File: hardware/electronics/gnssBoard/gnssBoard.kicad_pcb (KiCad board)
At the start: 4 copper layers, 0 parts

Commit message: worked on GNSS board
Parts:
- added AE1: CONMHF1-SMD-T, lib_fp:CONMHF1, F.Cu at (148.5, 80.5)
- added BT1: ~, lib_fp:MS621FE-FL11E, F.Cu at (132.9, 81.7)
- added C1: 2.2uF, lib_fp:MLCC0603, F.Cu at (147.7, 112.8)
- added C10: 10nF, lib_fp:MLCC0603, F.Cu at (146.3, 84.2)
- added C2: 2.2uF, lib_fp:MLCC0603, F.Cu at (142.2, 112.5)
- added C3: 1uF, lib_fp:MLCC0603, F.Cu at (130.2, 92.1)
- added C4: 100nF, lib_fp:MLCC0603, F.Cu at (130.2, 95.0)
- added C5: 100nF, lib_fp:MLCC0603, F.Cu at (130.2, 98.0)
- added C6: 1uF, lib_fp:MLCC0603, F.Cu at (130.2, 101.0)
- added C7: 100nF, lib_fp:MLCC0603, F.Cu at (130.2, 103.9)
- added C8: 2.2uF, lib_fp:MLCC0603, F.Cu at (135.8, 85.8)
- added C9: 47pF, lib_fp:MLCC0603, F.Cu at (149.8, 104.8)
- added D1: LTST-C190KYKT, lib_fp:LTST-0603, F.Cu at (130.0, 113.6)
- added D2: LTST-C190KGKT, lib_fp:LTST-0603, F.Cu at (140.2, 79.1)
- added D3: LTST-C190KRKT, lib_fp:LTST-0603, F.Cu at (140.2, 80.7)
- added D4: LTST-C190TBKT, lib_fp:LTST-0603, F.Cu at (149.8, 108.4)
- added D5: B0540WQ, lib_fp:SOD123, F.Cu at (138.6, 84.9)
- added D6: PTVS4V5D1BLYL, lib_fp:SOD882, F.Cu at (148.2, 83.6)
- added J2: M.2_E_Key_PCB_Edge, lib_fp:M.2 E-Key, F.Cu at (140.0, 120.0)
- added JP1: ~, lib_fp:Jumper_2_Bridged, B.Cu at (176.6, 100.8)
- added JP4: ~, lib_fp:Jumper_2_Bridged, B.Cu at (176.4, 104.5)
- added L1: 47nH, lib_fp:L_0402, F.Cu at (148.1, 85.0)
- added Q1: DMN2992UFB4Q-7B, lib_fp:XDFN3P35_100X60X40L15X25N, F.Cu at (135.6, 114.4)
- added Q2: DMN2992UFB4Q-7B, lib_fp:XDFN3P35_100X60X40L15X25N, F.Cu at (136.7, 114.4)
- added Q3: DMN2992UFB4Q-7B, lib_fp:XDFN3P35_100X60X40L15X25N, F.Cu at (134.5, 114.4)
- added Q4: DMN2992UFB4Q-7B, lib_fp:XDFN3P35_100X60X40L15X25N, F.Cu at (133.4, 114.4)
- added Q5: DMG1013TQ-7, lib_fp:SOT23-3P50_160X160X75L22X22N, F.Cu at (146.5, 86.8)
- added R1: 10K, lib_fp:CRCW0402, F.Cu at (144.8, 115.0)
- added R10: 4K7, lib_fp:CRCW0402, F.Cu at (134.5, 112.2)
- added R11: 4K7, lib_fp:CRCW0402, F.Cu at (133.4, 112.2)
- added R12: 4K7, lib_fp:CRCW0402, F.Cu at (120.9, 117.4)
- added R13: 4K7, lib_fp:CRCW0402, F.Cu at (120.9, 119.5)
- added R14: 4K7, lib_fp:CRCW0402, F.Cu at (149.8, 111.0)
- added R15: 3K3, lib_fp:CRCW0402, F.Cu at (135.3, 87.2)
- added R16: 10R, lib_fp:CRCW0603, F.Cu at (144.7, 85.8)
- added R17: 10K, lib_fp:CRCW0402, F.Cu at (148.2, 86.8)
- added R18: 1K, lib_fp:CRCW0402, F.Cu at (142.0, 86.5)
- added R19: 100K, lib_fp:CRCW0402, F.Cu at (140.2, 86.5)
- added R2: 10K, lib_fp:CRCW0402, F.Cu at (146.8, 115.0)
- added R20: 10K, lib_fp:CRCW0402, F.Cu at (140.8, 111.9)
- added R21: 27R, lib_fp:CRCW0402, F.Cu at (150.2, 113.5)
- added R22: 27R, lib_fp:CRCW0402, F.Cu at (149.0, 113.5)
- added R23: 10K, lib_fp:CRCW0402, F.Cu at (139.6, 111.9)
- added R3: 1K, lib_fp:CRCW0402, F.Cu at (130.5, 111.5)
- added R4: 4K7, lib_fp:CRCW0402, F.Cu at (137.6, 79.1)
- added R5: 4K7, lib_fp:CRCW0402, F.Cu at (137.6, 80.7)
- added R6: 4K7, lib_fp:CRCW0402, F.Cu at (136.7, 112.2)
- added R7: 4K7, lib_fp:CRCW0402, F.Cu at (135.6, 112.2)
- added R8: 4K7, lib_fp:CRCW0402, F.Cu at (119.2, 110.4)
- added R9: 4K7, lib_fp:CRCW0402, F.Cu at (119.2, 112.5)
- added TP1: ~, lib_fp:TP_1mm, B.Cu at (179.4, 83.8)
- added TP10: ~, lib_fp:TP_1mm, B.Cu at (177.4, 91.8)
- added TP11: ~, lib_fp:TP_1mm, B.Cu at (178.7, 95.2)
- added TP12: ~, lib_fp:TP_1mm, B.Cu at (178.7, 97.2)
- added TP13: ~, lib_fp:TP_1mm, B.Cu at (176.7, 95.2)
- added TP14: ~, lib_fp:TP_1mm, B.Cu at (176.7, 97.2)
- added TP15: ~, lib_fp:TP_1mm, B.Cu at (174.7, 95.2)
- added TP16: ~, lib_fp:TP_1mm, B.Cu at (174.7, 97.2)
- added TP2: ~, lib_fp:TP_1mm, B.Cu at (179.4, 85.8)
- added TP3: ~, lib_fp:TP_1mm, B.Cu at (179.4, 87.8)
- added TP4: ~, lib_fp:TP_1mm, B.Cu at (179.4, 89.8)
- added TP5: ~, lib_fp:TP_1mm, B.Cu at (179.4, 91.8)
- added TP6: ~, lib_fp:TP_1mm, B.Cu at (177.4, 83.8)
- added TP7: ~, lib_fp:TP_1mm, B.Cu at (177.4, 85.8)
- added TP8: ~, lib_fp:TP_1mm, B.Cu at (177.4, 87.8)
- added TP9: ~, lib_fp:TP_1mm, B.Cu at (177.4, 89.8)
- added U1: AP7361E, lib_fp:UDFN8P65_300X300X60L25X45L, F.Cu at (144.9, 112.8)
- added U2: ZED-F9P, lib_fp:ZED-F9P-04B_UBL, F.Cu at (140.0, 99.5)
- added U3: OPA344, lib_fp:SOT23-5P95_280X300X110L40X38N, F.Cu at (142.0, 84.0)
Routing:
- net +3V3: track 0.00 -> 79.1 mm, vias 0 -> 9
- net Net-(J2-~{LED_1}): track 0.00 -> 43.7 mm, vias 0 -> 3
- net Net-(J2-~{LED_2}): track 0.00 -> 43.4 mm, vias 0 -> 3
- net /GNSS Module/ANT_DET: track 0.00 -> 29.9 mm, vias 0 -> 2
- net /GNSS Module/ZED_D-: track 0.00 -> 27.6 mm, vias 0 -> 2
- net /GNSS Module/ZED_D+: track 0.00 -> 27.0 mm, vias 0 -> 2
- net VSS: track 0.00 -> 24.0 mm, vias 0 -> 94
- net /GNSS Module/ANT_SHORT_N: track 0.00 -> 21.9 mm, vias 0 -> 2
- net /GNSS Module/ANT_IN: track 0.00 -> 21.1 mm
- net VBAT: track 0.00 -> 19.4 mm, vias 0 -> 2
- net /PPS: track 0.00 -> 18.3 mm, vias 0 -> 1
- net /GNSS Module/ANT_OFF: track 0.00 -> 17.7 mm, vias 0 -> 2
- net VCC_RF: track 0.00 -> 16.4 mm, vias 0 -> 2
- net /ZED_RXD_1V8: track 0.00 -> 14.0 mm, vias 0 -> 3
- net /ZED_TXD_1V8: track 0.00 -> 13.2 mm, vias 0 -> 3
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- added copper zone on B.Cu, net +3V3
- added copper zone on F.Cu, net VSS
- added copper zone on In1.Cu, net VSS
- added copper zone on In2.Cu, net VSS
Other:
- board outline added: 22 x 36.8 mm

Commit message: finished first attempt at layout
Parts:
- removed JP1, JP4: ~, lib_fp:Jumper_2_Bridged
- removed TP1, TP10, TP11, TP12, TP13, TP14, TP15, TP16, TP2, TP3, TP4, TP5, TP6, TP7, TP8, TP9: ~, lib_fp:TP_1mm
- moved R9 15.8 mm to (134.7, 115.4)
- moved R8 13.1 mm to (131.6, 114.9), turned to -90 degrees
- moved R13 13.1 mm to (130.2, 110.2)
- moved R12 12.1 mm to (132.7, 114.9), turned to -90 degrees
- moved Q1 3.51 mm to (138.6, 112.5)
- moved Q4 2.62 mm to (132.1, 112.1)
- moved Q3 0.65 mm to (133.9, 114.0)
- moved Q2 0.65 mm to (136.2, 114.0)
- moved R3 0.33 mm to (130.2, 111.4)
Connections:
- D1 pad 2: Net-(D1-Pad2) -> VSS
- D4 pad 2: Net-(D4-Pad2) -> VSS
- J2 pad 40: /RESET_N -> /EXTINT
- J2 pad 42: /EXTINT -> /RESET_N
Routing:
- net +3V3: track 79.1 -> 129.6 mm, vias 9 -> 11
- net +1V8: track 12.1 -> 38.4 mm, vias 4 -> 5
- net /SCL_1V8: track 4.58 -> 17.3 mm, vias 1 -> 2
- net VSS: track 24.0 -> 36.7 mm, vias 94 -> 93
- net /ZED_TXD_1V8: track 13.2 -> 20.2 mm, vias 3 -> 4
- net /GNSS Module/SDA_3V3: track 2.29 -> 6.08 mm, vias 1 -> 2
- net /GNSS Module/SCL_3V3: track 2.29 -> 5.34 mm, vias 1 -> 2
- net /ZED_RXD_1V8: track 14.0 -> 16.3 mm, vias 3 -> 4
- net /GNSS Module/ZED_TXD_3V3: track 5.41 -> 3.59 mm, vias 2 -> 0
- net /SDA_1V8: track 5.12 -> 6.15 mm
- net /EXTINT: track 12.4 -> 11.5 mm
- removed copper zone on B.Cu, net +3V3

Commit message: finished routing and passed DRC
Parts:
- added J1: VAL, lib_fp:M.2-Screw-Pad, F.Cu at (140.0, 78.0)
- moved D2 5.53 mm to (145.3, 81.2), turned to 90 degrees
- moved R5 4.92 mm to (142.2, 82.5), turned to -90 degrees
- moved R4 4.77 mm to (141.0, 82.5), turned to -90 degrees
- moved D3 3.44 mm to (143.6, 81.2), turned to 90 degrees
- moved R18 1.42 mm to (142.9, 87.6)
- moved U3 1.25 mm to (141.9, 85.3)
- moved R19 1.14 mm to (140.7, 87.6), turned to 180 degrees
- moved D5 0.46 mm to (138.6, 85.4)
- moved C9 0.30 mm to (149.8, 104.5)
- moved D4 0.05 mm to (149.8, 108.3)
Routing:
- net Net-(D2-Pad1): track 1.36 -> 7.63 mm, vias 0 -> 2
- net Net-(J2-~{LED_1}): track 43.7 -> 38.3 mm
- net +3V3: track 129.6 -> 124.6 mm, vias 11 -> 10
- net Net-(J2-~{LED_2}): track 43.4 -> 39.9 mm
- net /GNSS Module/ANT_DET: track 29.9 -> 30.8 mm
- net /GNSS Module/ANT_SHORT_N: track 21.9 -> 22.6 mm
- net Net-(D3-Pad1): track 1.36 -> 2.09 mm
- net /GNSS Module/SDA_3V3: track 6.08 -> 6.72 mm
- net VSS: vias 93 -> 96

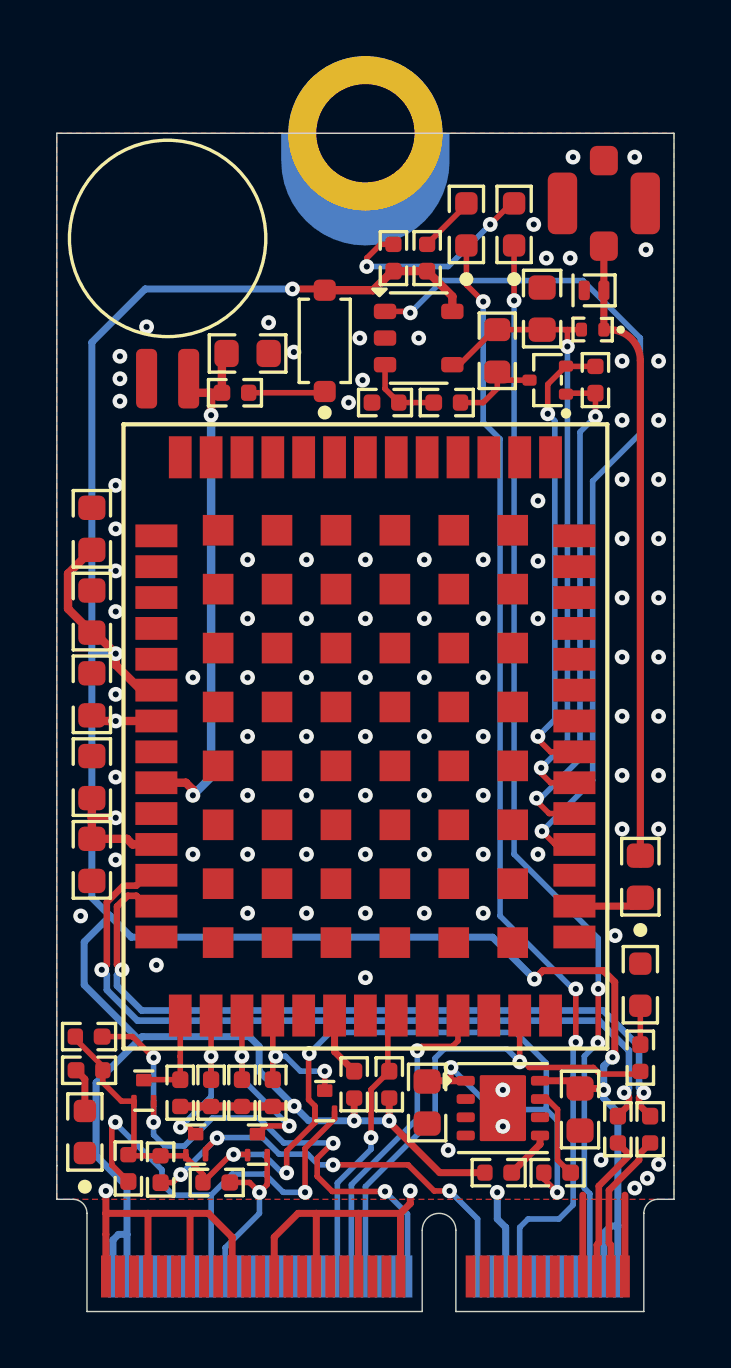
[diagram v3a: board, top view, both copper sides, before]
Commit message: replaced MOSFETS with level shifter and cleaned up routing. added silkscreen text
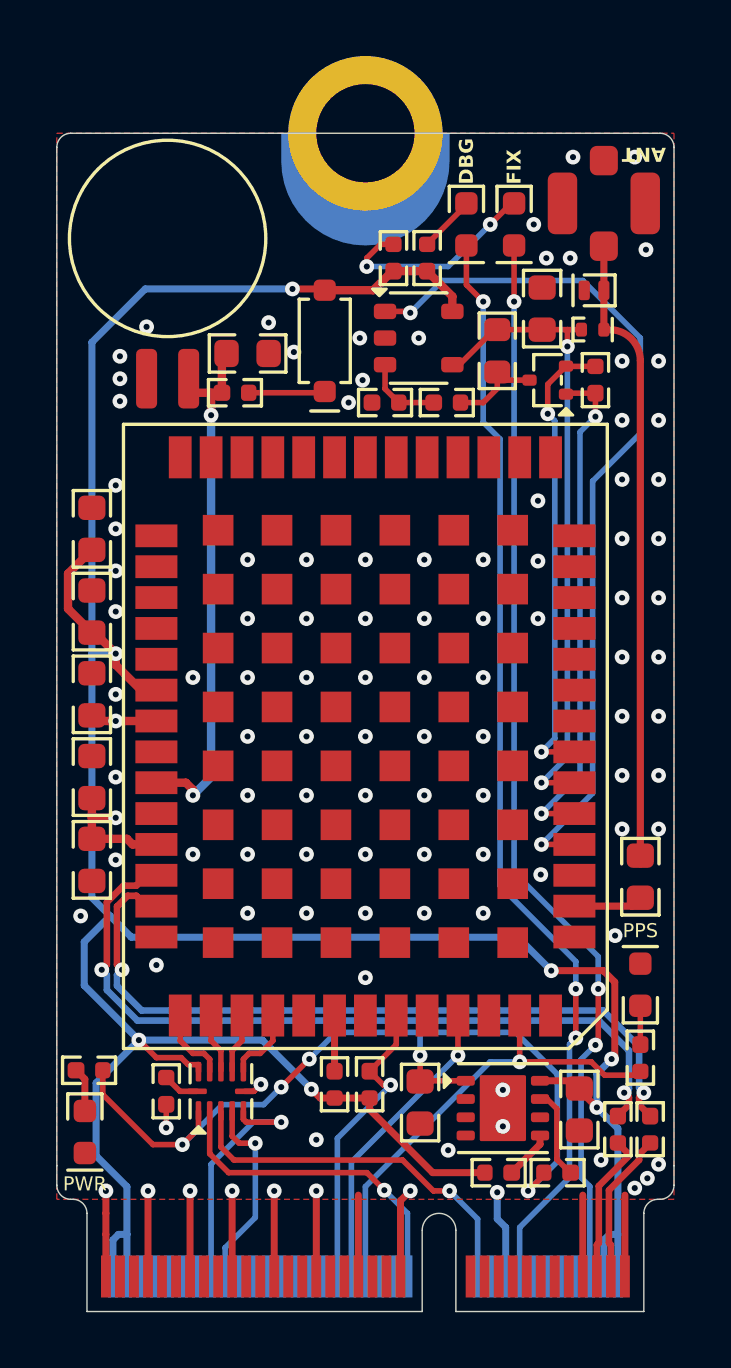
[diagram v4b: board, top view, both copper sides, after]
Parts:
- removed Q1, Q2, Q3, Q4: DMN2992UFB4Q-7B, lib_fp:XDFN3P35_100X60X40L15X25N
- removed R10, R11, R12, R13, R7, R8, R9: 4K7, lib_fp:CRCW0402
- added REF**: OSHW-Logo2_7.3x6mm_SilkScreen, DS-Logos-and-Graphics:OSHW-Logo2_7.3x6mm_SilkScreen, B.Cu at (140.0, 109.0)
- added U4: TXS0104VxRUTR, lib_fp:RUT0012A, F.Cu at (134.8, 112.2)
- R6: value 4K7 -> 10K
- moved R6 3.80 mm to (132.9, 112.2), turned to -90 degrees
- moved R20 0.70 mm to (140.2, 111.9)
- moved R23 0.70 mm to (138.9, 111.9)
- moved C2 0.25 mm to (141.9, 112.5)
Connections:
- R6 pad 1: +3V3 -> Net-(U4-OE)
- R6 pad 2: /GNSS Module/SCL_3V3 -> VSS
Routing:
- net /ZED_TXD_1V8: track 20.4 -> 11.7 mm, vias 4 -> 1
- net /SCL_1V8: track 17.4 -> 8.81 mm, vias 2 -> 1
- net +1V8: track 38.4 -> 30.4 mm
- net /GNSS Module/SDA_3V3: track 6.72 -> 2.09 mm, vias 2 -> 0
- net /GNSS Module/ZED_RXD_3V3: track 5.91 -> 2.09 mm, vias 2 -> 0
- net +3V3: track 124.6 -> 121.0 mm, vias 10 -> 9
- net /ZED_RXD_1V8: track 16.0 -> 13.5 mm, vias 4 -> 1
- net /GNSS Module/SCL_3V3: track 5.03 -> 2.67 mm, vias 2 -> 0
- net VSS: track 36.7 -> 34.8 mm, vias 96 -> 104
- net /PPS: track 18.3 -> 16.7 mm
- net Net-(U4-OE): track 0.00 -> 1.30 mm
- net /RESET_N: track 10.2 -> 11.4 mm
- net /SDA_1V8: track 6.15 -> 7.02 mm
- net Net-(J2-~{LED_2}): track 39.9 -> 39.2 mm
- net /EXTINT: track 11.5 -> 10.9 mm
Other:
- outline, holes or cut-outs redrawn
- board text added: "ANT"
- board text added: "DBG"
- board text added: "FIX"
- board text added: "PPS"
- board text added: "PWR"
- board text added: "ZED-F9P GNSS M.2 E-Key Card Embry-Riddle Aeronautical University Physical Sciences Department Madison Gleydura Master's Thesis 2024-12-01"

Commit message: re-added cut traces and test points and flxed keepout for edge connector
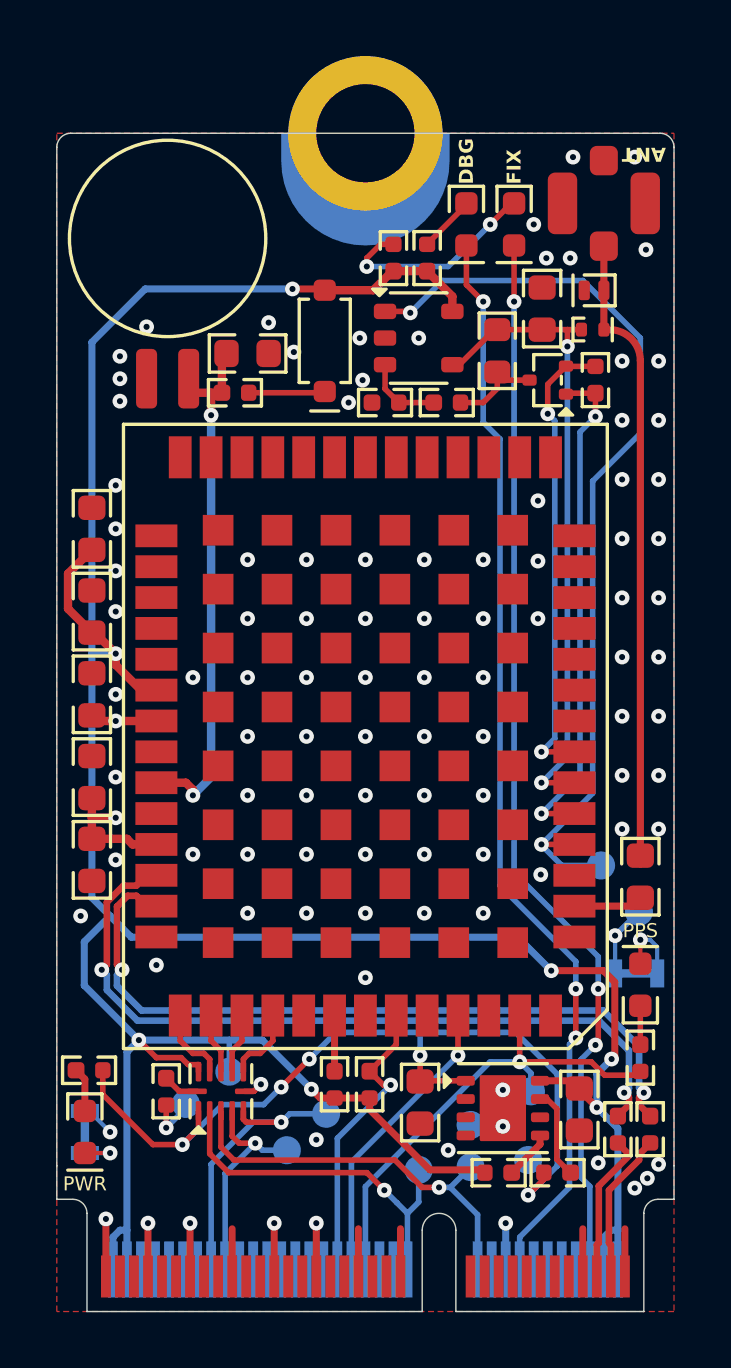
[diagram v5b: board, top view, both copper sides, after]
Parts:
- added JP1: ~, lib_fp:Jumper_2_Bridged, B.Cu at (130.0, 113.6)
- added JP2: ~, lib_fp:Jumper_2_Bridged, B.Cu at (149.7, 108.0)
- added TP1: ~, lib_fp:TP_1mm, B.Cu at (135.2, 111.5)
- added TP10: ~, lib_fp:TP_1mm, B.Cu at (148.4, 104.1)
- added TP11: ~, lib_fp:TP_1mm, B.Cu at (149.8, 105.8)
- added TP2: ~, lib_fp:TP_1mm, B.Cu at (145.8, 114.6)
- added TP3: ~, lib_fp:TP_1mm, B.Cu at (143.8, 114.8)
- added TP4: ~, lib_fp:TP_1mm, B.Cu at (141.9, 115.0)
- added TP5: ~, lib_fp:TP_1mm, B.Cu at (137.2, 114.2)
- added TP6: ~, lib_fp:TP_1mm, B.Cu at (138.6, 113.0)
- added TP7: ~, lib_fp:TP_1mm, B.Cu at (133.6, 112.6)
- added TP8: ~, lib_fp:TP_1mm, B.Cu at (143.8, 113.3)
- added TP9: ~, lib_fp:TP_1mm, B.Cu at (145.9, 112.2)
- J1: value VAL -> Standoff
- turned R6 to 90 degrees
- renumbered Q5 to Q1, R16 to R10, R21 to R11, R22 to R12, R17 to R13, R23 to R14, R18 to R15, R19 to R16, R14 to R7, R20 to R8, R15 to R9, U4 to U2, U2 to U3, U3 to U4
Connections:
- D1 pad 2: VSS -> Net-(D1-Pad2)
- D4 pad 2: VSS -> Net-(D4-Pad2)
- R6 pad 1: Net-(U4-OE) -> VSS
- R6 pad 2: VSS -> Net-(U2-OE)
- U2 pad 12: Net-(U4-OE) -> Net-(U2-OE)
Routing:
- net VSS: track 34.8 -> 27.4 mm, vias 104 -> 103
- net Net-(D4-Pad2): track 0.00 -> 2.50 mm, vias 0 -> 1
- net /GNSS Module/ANT_DET: track 31.1 -> 33.6 mm
- net Net-(D1-Pad2): track 0.00 -> 1.80 mm, vias 0 -> 1
- net /SCL_1V8: track 8.81 -> 10.3 mm
- net /ZED_TXD_1V8: track 11.7 -> 13.2 mm
- net Net-(U4-OE): track 1.30 -> 0.00 mm
- net Net-(U2-OE): track 0.00 -> 1.29 mm
- net /SDA_1V8: track 7.02 -> 8.25 mm
- net +1V8: track 30.4 -> 31.6 mm
- net /PPS: track 16.7 -> 17.7 mm
- net /ZED_RXD_1V8: track 13.5 -> 14.4 mm
- net +3V3: track 121.0 -> 120.5 mm
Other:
- board text added: "ZED-F9P GNSS M.2 E-Key Card Embry-Riddle Aeronautical University Physical Sciences Department Madison Gleydura Master's Thesis 2024-12-02"
- board text removed: "ZED-F9P GNSS M.2 E-Key Card Embry-Riddle Aeronautical University Physical Sciences Department Madison Gleydura Master's Thesis 2024-12-01"

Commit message: moved around vendor defined and reset line
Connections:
- J2 pad 42: /RESET_N -> /TX_RDY
- J2 pad 52: unconnected-(J2-~{PERST0}-Pad52) -> /RESET_N
- U3 pad 46: unconnected-(U3-TX_RDY-Pad46) -> /TX_RDY
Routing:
- net /TX_RDY: track 0.00 -> 24.2 mm, vias 0 -> 3
- net /RESET_N: track 11.1 -> 12.7 mm

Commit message: renumbered resistors. cleaned up tracks
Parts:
- removed the R8 at (140.2, 111.9)
- removed REF**: OSHW-Logo2_7.3x6mm_SilkScreen, DS-Logos-and-Graphics:OSHW-Logo2_7.3x6mm_SilkScreen
- renumbered R11 to R10, R12 to R11, R13 to R12, R14 to R13, R15 to R14, R16 to R15, R9 to R8, R10 to R9
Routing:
- net /RESET_N: track 12.7 -> 11.9 mm
